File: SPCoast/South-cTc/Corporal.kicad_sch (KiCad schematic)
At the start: 1 part

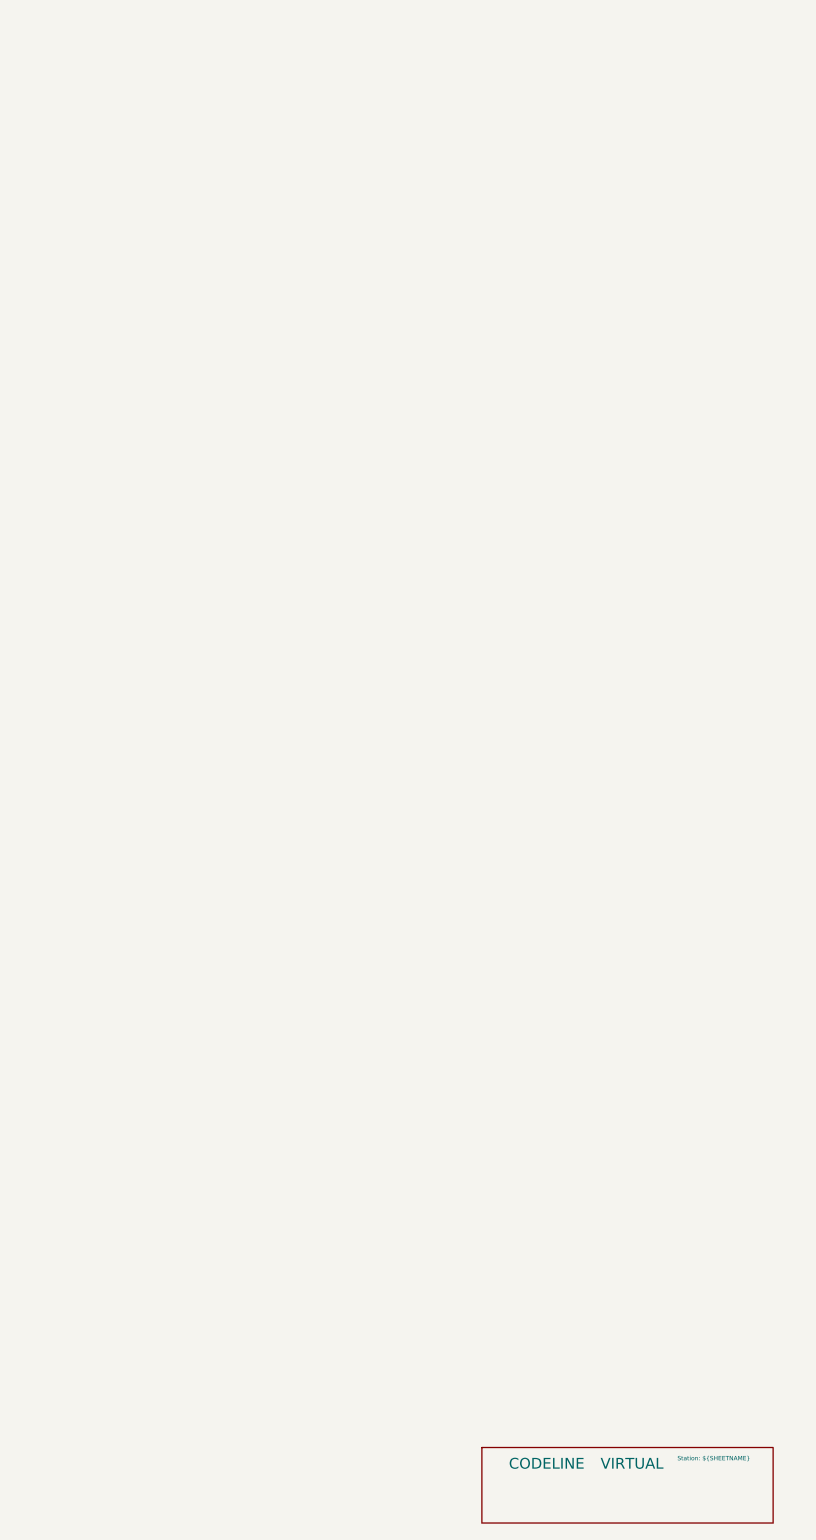
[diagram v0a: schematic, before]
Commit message: SPCoast: derail pin R, track circuit names end in T, code line symbols on the root sheet
Working-tree changes from the 2026-10-01..03 vocabulary review with
FieldUnit-Subdivision (docs/adr/0001-code-line-type-contract.md):

- Switch_Powered_Derail pin 2 is R (through path = REVERSE) in the seven
  plant schematics (library Railroad.kicad_sym renamed alongside; not in git)
- Luchessa track circuits renamed to end in T (1SAT, 2NAAT, ...); MC1 moved
  to CP Gilroy's house
- South-cTc: transports (MQTT, TimeCode, CMRInet, Loconet) on the root
  sheet on the CtcMachine Transports pin; field stations as encoding
  instances on the Luchessa sheet; two Luchessa lamp tokens renamed
- Six plant projects (Christopher, Corporal, GilroyCalTrain,
  GilroyInterchange, Sargent, Watsonville) added as drawn so far; Watsonville
  updated 2026-10-02

Co-Authored-By: Claude Fable 5.1 <noreply@anthropic.com>
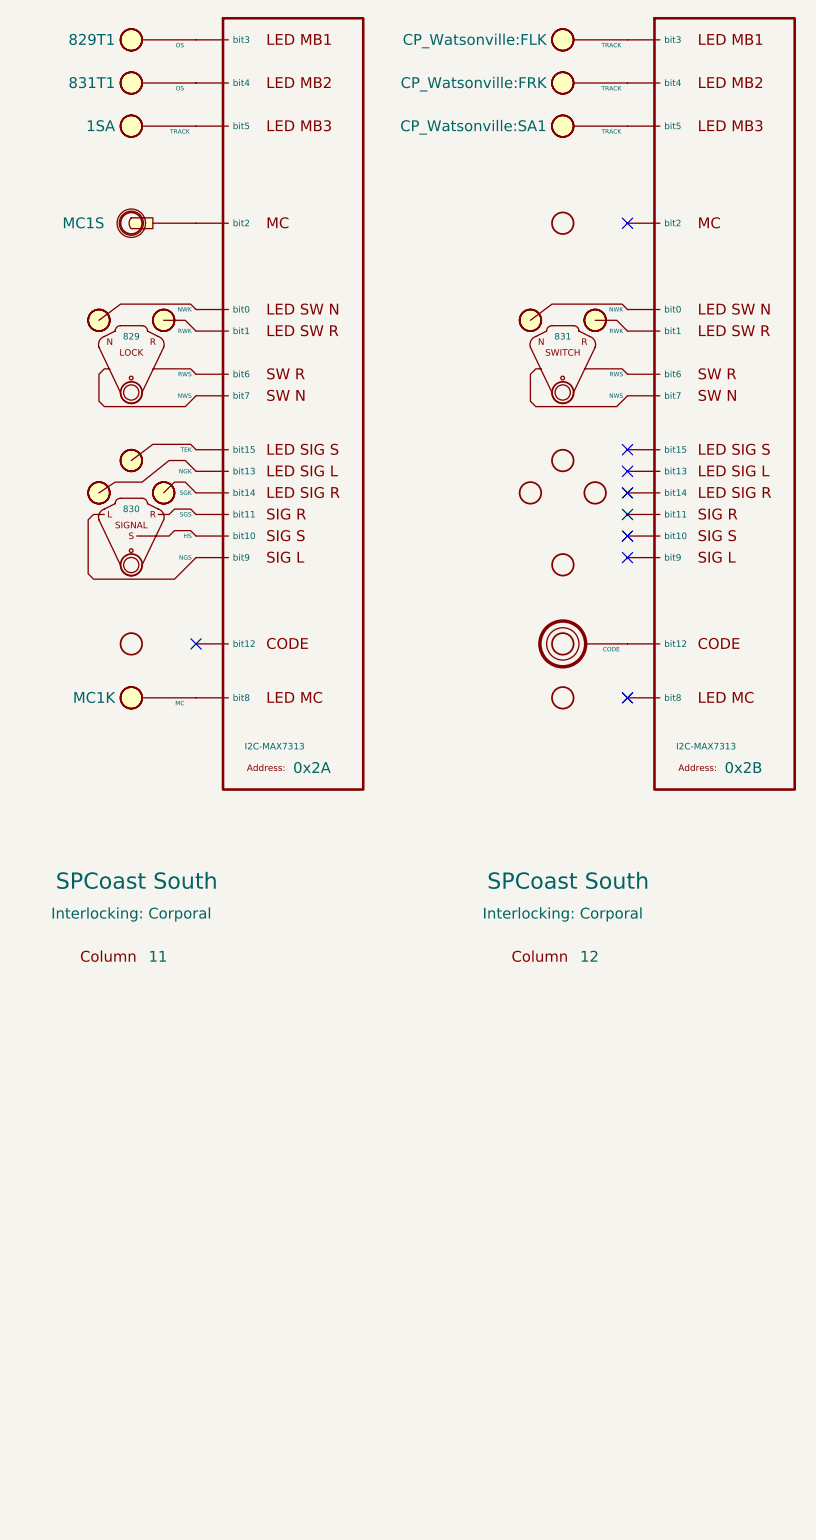
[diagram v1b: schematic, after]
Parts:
- removed CODELINE5: VIRTUAL, symbol RailroadPanel:Codeline-Virtual
- added CDE12: CODE, symbol RailroadPanel:PanelCode
- added COL31: 11, symbol RailroadPanel:PanelColumn
- added COL32: 12, symbol RailroadPanel:PanelColumn
- added LKL11: 829, symbol RailroadPanel:PanelLock
- added LMP111: OS, symbol RailroadPanel:PanelLamp-YELLOW
- added LMP112: OS, symbol RailroadPanel:PanelLamp-RED
- added LMP113, LMP123: TRACK, symbol RailroadPanel:PanelLamp-YELLOW
- added LMP121, LMP122: TRACK, symbol RailroadPanel:PanelLamp-BLUE
- added MCK11: MC, symbol RailroadPanel:PanelLamp-YELLOW
- added MCL11: MC1, symbol RailroadPanel:PanelMCall
- added SGL11: 830, symbol RailroadPanel:PanelSignal
- added SWL12: 831, symbol RailroadPanel:PanelSwitch
- added U31: 0x2A, symbol RailroadPanel:PanelColumn-MAX7313
- added U32: 0x2B, symbol RailroadPanel:PanelColumn-MAX7313
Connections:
- new net: COL31.1 (Column), LMP111.1 (Column)
- new net: LMP111.2 (LAMP), U31.4 (bit3)
- new net: COL32.3 (Column), LMP123.1 (Column)
- new net: LMP123.2 (LAMP), U32.6 (bit5)
- new net: LKL11.5 (NWK), U31.1 (bit0)
- new net: SGL11.2 (NGS), U31.10 (bit9)
- new net: SGL11.3 (HS), U31.11 (bit10)
- new net: SGL11.4 (SGS), U31.12 (bit11)
- new net: SGL11.6 (NGK), U31.14 (bit13)
- new net: SGL11.5 (SGK), U31.15 (bit14)
- new net: SGL11.7 (TEK), U31.16 (bit15)
- new net: LKL11.4 (RWK), U31.2 (bit1)
- new net: MCL11.2 (SW), U31.3 (bit2)
- new net: LMP112.2 (LAMP), U31.5 (bit4)
- new net: LMP113.2 (LAMP), U31.6 (bit5)
- new net: LKL11.3 (RWS), U31.7 (bit6)
- new net: LKL11.2 (NWS), U31.8 (bit7)
- new net: MCK11.2 (LAMP), U31.9 (bit8)
- new net: COL31.3 (Column), LMP113.1 (Column)
- new net: COL31.8 (Column), MCK11.1 (Column)
- new net: COL32.1 (Column), LMP121.1 (Column)
- new net: LMP121.2 (LAMP), U32.4 (bit3)
- new net: SWL12.5 (NWK), U32.1 (bit0)
- new net: CDE12.2 (CODE), U32.13 (bit12)
- new net: SWL12.4 (RWK), U32.2 (bit1)
- new net: LMP122.2 (LAMP), U32.5 (bit4)
- new net: SWL12.3 (RWS), U32.7 (bit6)
- new net: SWL12.2 (NWS), U32.8 (bit7)
- new net: COL32.5 (Column), SWL12.1 (Column)
- new net: COL32.2 (Column), LMP122.1 (Column)
- new net: COL31.2 (Column), LMP112.1 (Column)
- new net: COL31.4 (Column), MCL11.1 (Column)
- new net: COL31.5 (Column), LKL11.1 (Column)
- new net: COL31.6 (Column), SGL11.1 (Column)
- new net: CDE12.1 (Column), COL32.7 (Column)
- no-connect marks 0 -> 9

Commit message: SPCoast: Address field and Kind on PanelColumn-MAX7313; encoding Values; HBA; Watsonville update
Owner's drawing changes of 2026-10-02..03 (FieldUnit-Subdivision ADR 0002 D18
and the owner's responses):

- PanelColumn-MAX7313: the expander address moves from the Value to an
  Address field (Value is ${Address}); BusKind renamed Kind (I2C-MAX7313)
- Luchessa encoding symbols: Value "US&S 506 time-coded DC pulses"
- Sargent: HBD renamed HBA; traffic indications [NSEW]FLK
- Watsonville schematic brought to a usable state
- Luchessa plant: track circuits end in T; MC1 at CP Gilroy's house

Co-Authored-By: Claude Fable 5.1 <noreply@anthropic.com>
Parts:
- LMP121: IndicationToken CP_Watsonville:FLK -> CP_Watsonville:NFLK
- LMP122: IndicationToken CP_Watsonville:FRK -> CP_Watsonville:SFLK
- U31: Address (none) -> 0x2A; BusKind I2C-MAX7313 -> (none); Kind (none) -> I2C-MAX7313
- U32: Address (none) -> 0x2B; BusKind I2C-MAX7313 -> (none); Kind (none) -> I2C-MAX7313
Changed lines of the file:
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@@
 		(property "Value" "0x2A"
 			(at 99.06 112.395 0)
+			(hide yes)
 			(show_name no)
 			(do_not_autoplace yes)
@@
 			)
 		)
-		(property "BusKind" "I2C-MAX7313"
+		(property "Role" "IODRIVER"
+			(at 97.79 107.315 0)
+			(hide yes)
+			(show_name no)
+			(do_not_autoplace no)
+			(effects
+				(font
+					(size 1.27 1.27)
+				)
+			)
+		)
+		(property "Kind" "I2C-MAX7313"
 			(at 93.345 109.855 0)
 			(show_name no)
-			(do_not_autoplace yes)
+			(do_not_autoplace no)
 			(effects
 				(font
@@
 			)
 		)
-		(property "Role" "IODRIVER"
-			(at 99.06 72.39 0)
-			(hide yes)
+		(property "Address" "0x2A"
+			(at 101.092 112.522 0)
 			(show_name no)
 			(do_not_autoplace no)
@@
 			)
 		)
-		(property "IndicationToken" "CP_Watsonville:FLK"
+		(property "IndicationToken" "CP_Watsonville:NFLK"
 			(at 128.905 26.67 0)
 			(show_name no)
@@
 		(property "Value" "0x2B"
 			(at 149.86 112.395 0)
+			(hide yes)
 			(show_name no)
 			(do_not_autoplace yes)
@@
 			)
 		)
-		(property "BusKind" "I2C-MAX7313"
+		(property "Role" "IODRIVER"
+			(at 148.59 107.315 0)
+			(hide yes)
+			(show_name no)
+			(do_not_autoplace no)
+			(effects
+				(font
+					(size 1.27 1.27)
+				)
+			)
+		)
+		(property "Kind" "I2C-MAX7313"
 			(at 144.145 109.855 0)
 			(show_name no)
-			(do_not_autoplace yes)
+			(do_not_autoplace no)
 			(effects
 				(font
@@
 			)
 		)
-		(property "Role" "IODRIVER"
-			(at 149.86 72.39 0)
-			(hide yes)
+		(property "Address" "0x2B"
+			(at 152.4 112.522 0)
 			(show_name no)
 			(do_not_autoplace no)
@@
 			)
 		)
-		(property "IndicationToken" "CP_Watsonville:FRK"
+		(property "IndicationToken" "CP_Watsonville:SFLK"
 			(at 128.905 31.75 0)
 			(show_name no)

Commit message: fix(kicad): approach circuits end in T; desk tokens follow
Plants: Christopher 1NA/2NA/1SA/2SA, GilroyCalTrain 1NA/1SA, GilroyInterchange
1SA, Sargent 1NA/1SA/2SA gain the final T (ADR 0003 D4). Sargent's reference
Corporal:2NA becomes Corporal:2NAT, the circuit Corporal draws.

Desk (South-cTc sheets): IndicationToken follows the plants for Christopher,
GilroyCalTrain, GilroyInterchange; Corporal 1SA becomes 1SAT (the plant already
had it); Christopher 815T2 becomes 815AT1 (the OS circuit of switch 815A).

Not changed, awaiting decisions in the dry-run report: 0<n>T renames (IND,
TK<n>, Interchange, 2NAAT, 2SAT), section 2 of an approach, unnamed circuits,
Watsonville, CP_Watsonville: references, 1TK.

Verified: netlists rebuilt for all affected projects; of 33 desk circuit tokens,
5 now match no plant circuit (was 11): 1TK, CP_Watsonville:SA1,
CP_Watsonville:837T1, Watsonville 1NAK and 2NAK. KiCad closed, no ~*.lck.

Co-Authored-By: Claude Sonnet 5.5 <noreply@anthropic.com>
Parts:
- LMP113: IndicationToken 1SA -> 1SAT
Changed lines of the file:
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@@
 			)
 		)
-		(property "IndicationToken" "1SA"
+		(property "IndicationToken" "1SAT"
 			(at 78.105 36.83 0)
 			(show_name no)

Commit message: SPCoast: owner's edits: Watsonville virtual indications 0100T and 0101T, circuits 01T..03T, desk tokens (baseline)
Includes typos in the member lists (a period for a comma, a missing 25T1, a stray 03T), corrected in the next commit.

Co-Authored-By: Claude Sonnet 5.5 <noreply@anthropic.com>
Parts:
- LMP121: IndicationToken CP_Watsonville:NFLK -> Watsonville:NFLK
- LMP122: IndicationToken CP_Watsonville:SFLK -> Watsonville:SFLK
- LMP123: IndicationToken CP_Watsonville:SA1 -> Watsonville:02T
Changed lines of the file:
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@@
 			)
 		)
-		(property "IndicationToken" "CP_Watsonville:SA1"
+		(property "IndicationToken" "Watsonville:02T"
 			(at 128.905 36.83 0)
 			(show_name no)
@@
 			)
 		)
-		(property "IndicationToken" "CP_Watsonville:NFLK"
+		(property "IndicationToken" "Watsonville:NFLK"
 			(at 128.905 26.67 0)
 			(show_name no)
@@
 			)
 		)
-		(property "IndicationToken" "CP_Watsonville:SFLK"
+		(property "IndicationToken" "Watsonville:SFLK"
 			(at 128.905 31.75 0)
 			(show_name no)

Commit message: chore(kicad): refresh instances to the ADR 0003 libraries (InterlockingPlant 95f53e2)
- Desk sheets (South-cTc/*) and the Sargent sandbox: embedded PanelSwitch, PanelLock,
  PanelSignal, PanelMCall, PanelCode, PanelLamp-*, PanelColumn-MAX7313 definitions refreshed
  from the library (refresh_embedded.py, checked against the pre-pass library: only Description
  text had drifted). Instance Role APPLIANCE -> PANEL (77).
- Plant sheets: powered-switch instance Kind SWITCH_POWERED -> SWITCH_REMOTE (21), matching the
  library (sweep_role_kind_fields.py).

Verified:
- verify_symbol_diff.py: same symbols, lib_ids and positions; only Role/Kind changed.
- Nets unchanged: Christopher 30, Corporal 27, GilroyCalTrain 28, GilroyInterchange 23,
  Luchessa 35, Sargent 61, Watsonville 99, South-cTc 341.
- parse_kicad_plant.py --format text identical before/after for all seven plants.
- Desk compile 75/137/14, diagnostics identical; the 7 desk locks bind WLS/~{WLS}/~{WLK}/WLK
  to the bits that were NWS/RWS/RWK/NWK.
- No sheet or project outside Luchessa carries the copied root UUID.

Co-Authored-By: Claude Opus 5.5 <noreply@anthropic.com>
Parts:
- CDE12, LKL11, LMP111, LMP112, LMP113, LMP121, LMP122, LMP123, MCK11, MCL11, SGL11, SWL12: Role APPLIANCE -> PANEL
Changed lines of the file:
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@@
 			)
 		)
-		(property "Role" "APPLIANCE"
+		(property "Role" "PANEL"
 			(at 80.01 24.13 0)
 			(hide yes)
@@
 			)
 		)
-		(property "Role" "APPLIANCE"
+		(property "Role" "PANEL"
 			(at 130.81 34.29 0)
 			(hide yes)
@@
 			)
 		)
-		(property "Role" "APPLIANCE"
+		(property "Role" "PANEL"
 			(at 80.01 34.29 0)
 			(hide yes)
@@
 			)
 		)
-		(property "Role" "APPLIANCE"
+		(property "Role" "PANEL"
 			(at 80.01 101.6 0)
 			(hide yes)
@@
 			)
 		)
-		(property "Role" "APPLIANCE"
+		(property "Role" "PANEL"
 			(at 130.81 29.21 0)
 			(hide yes)
@@
 			)
 		)
-		(property "Role" "APPLIANCE"
+		(property "Role" "PANEL"
 			(at 131.445 76.2 0)
 			(hide yes)
@@
 			)
 		)
-		(property "Role" "APPLIANCE"
+		(property "Role" "PANEL"
 			(at 130.81 34.29 0)
 			(hide yes)
@@
 			)
 		)
-		(property "Role" "APPLIANCE"
+		(property "Role" "PANEL"
 			(at 80.01 34.29 0)
 			(hide yes)
@@
 			)
 		)
-		(property "Role" "APPLIANCE"
+		(property "Role" "PANEL"
 			(at 80.645 74.93 0)
 			(hide yes)
@@
 			)
 		)
-		(property "Role" "APPLIANCE"
+		(property "Role" "PANEL"
 			(at 86.36 44.45 0)
 			(hide yes)
@@
 			)
 		)
-		(property "Role" "APPLIANCE"
+		(property "Role" "PANEL"
 			(at 80.01 92.71 0)
 			(hide yes)
@@
 			)
 		)
-		(property "Role" "APPLIANCE"
+		(property "Role" "PANEL"
 			(at 130.81 90.17 0)
 			(hide yes)

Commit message: chore(kicad): desk sheets to Driver-I2C-MAX7313 and the PanelLock Kind (InterlockingPlant owner review)
- 14 desk expanders: lib_id RailroadPanel:PanelColumn-MAX7313 -> Driver-I2C-MAX7313, embedded
  definition refreshed (pins A1..B8, same numbers and positions).
- 8 PanelLock instances: Kind LOCK_LEVER -> LOCK_LEVER_2LAMP_2CONTACT (7 desk, 1 Sargent sandbox).

Verified:
- verify_symbol_diff.py: only those lib_id and Kind changes.
- South-cTc 341 nets, Sargent 61; desk compile 75/137/14 with bindings identical to e2c1093.

Co-Authored-By: Claude Opus 5.5 <noreply@anthropic.com>
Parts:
- LKL11: Kind LOCK_LEVER -> LOCK_LEVER_2LAMP_2CONTACT
- U31, U32: symbol RailroadPanel:PanelColumn-MAX7313 -> RailroadPanel:Driver-I2C-MAX7313
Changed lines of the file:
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@@
 	)
 	(symbol
-		(lib_id "RailroadPanel:PanelColumn-MAX7313")
+		(lib_id "RailroadPanel:Driver-I2C-MAX7313")
 		(at 99.06 72.39 0)
 		(unit 1)
@@
 	)
 	(symbol
-		(lib_id "RailroadPanel:PanelColumn-MAX7313")
+		(lib_id "RailroadPanel:Driver-I2C-MAX7313")
 		(at 149.86 72.39 0)
 		(unit 1)
@@
 			)
 		)
-		(property "Kind" "LOCK_LEVER"
+		(property "Kind" "LOCK_LEVER_2LAMP_2CONTACT"
 			(at 80.645 73.025 0)
 			(hide yes)
